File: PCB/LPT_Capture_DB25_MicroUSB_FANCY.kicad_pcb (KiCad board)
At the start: 2 copper layers, 36 x 20.8 mm, 21 parts, among them J1 USB3155-30-A, J2 DB25P064TXLF, Q1 SL2301S, Q2 SL2301S, U1 FT245RL

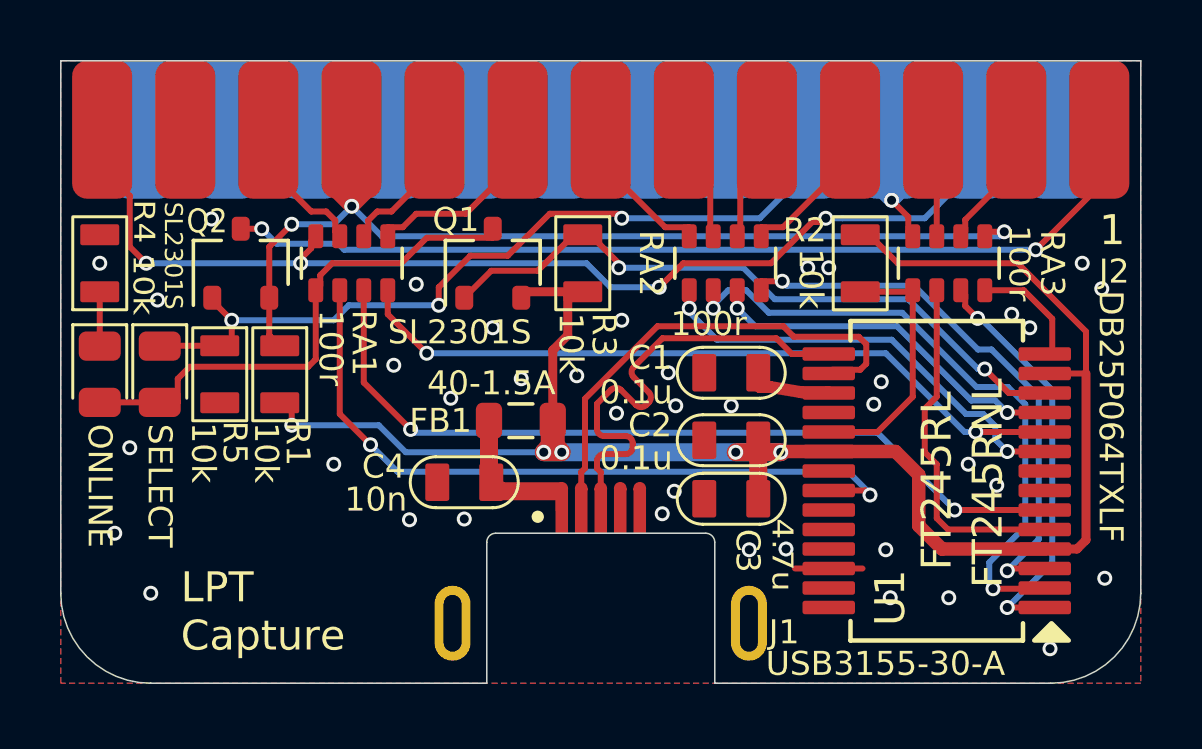
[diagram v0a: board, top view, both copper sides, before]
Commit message: fix db25_microusb_fancy filenames, pull db25_usbc_fancy into main
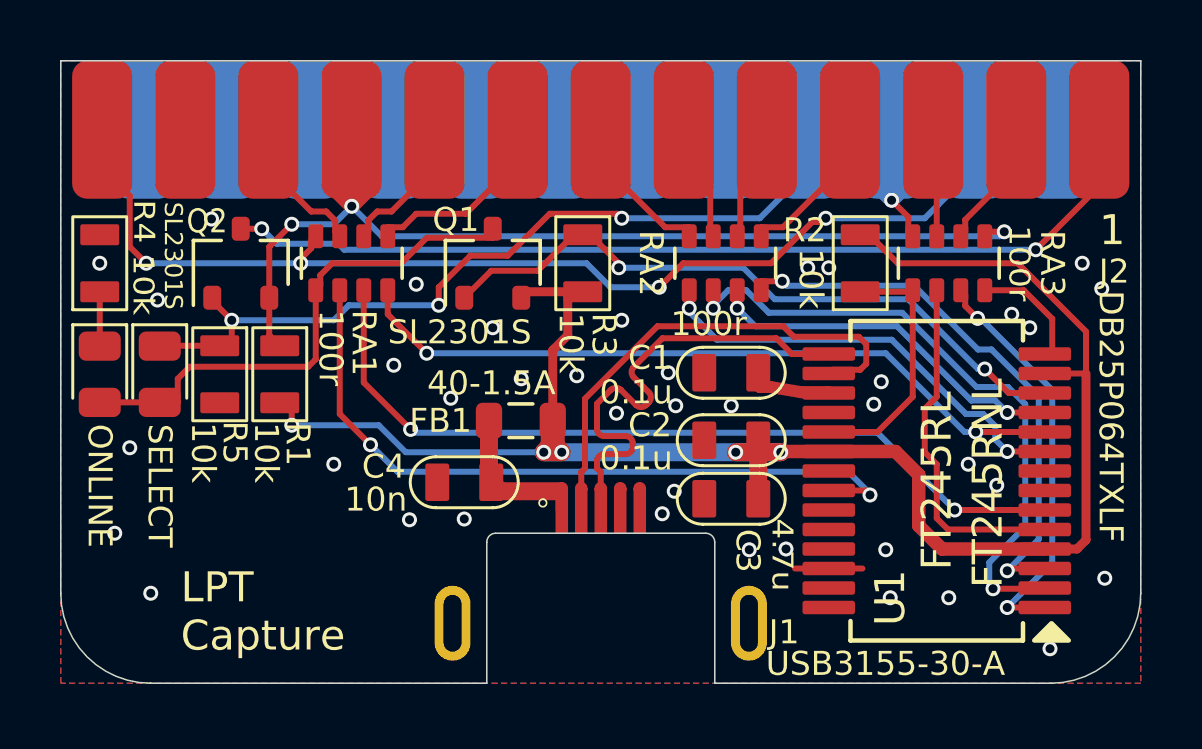
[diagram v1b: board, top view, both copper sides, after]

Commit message: pull c36_usbc_fancy into main
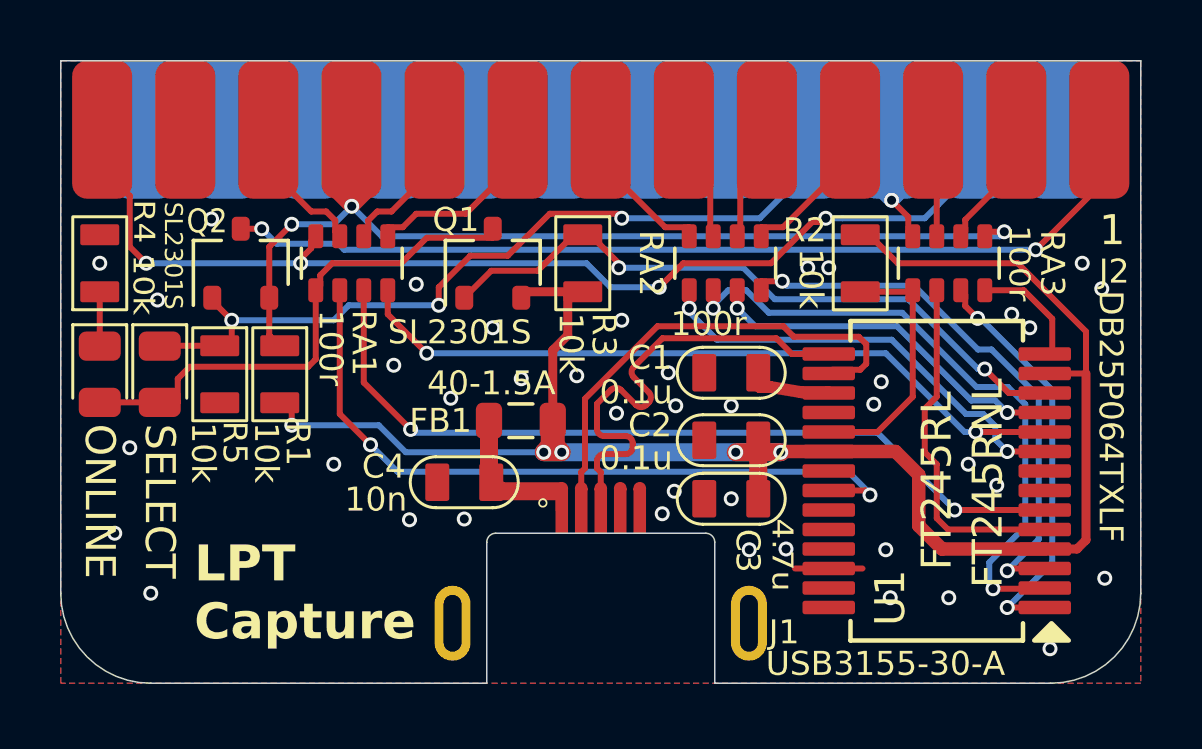
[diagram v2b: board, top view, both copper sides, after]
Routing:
- net GND: vias 39 -> 40

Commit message: db25-microusb-fancy add R6 current limit led when /SELIN driven low
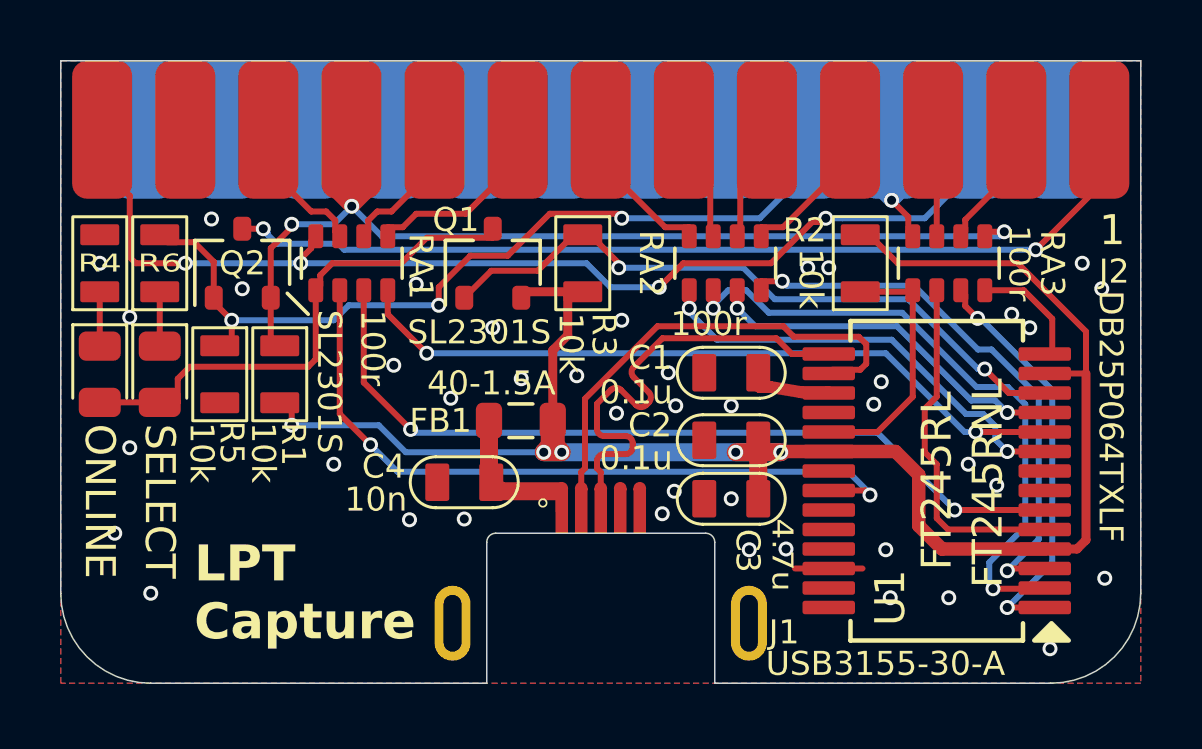
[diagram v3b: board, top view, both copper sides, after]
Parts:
- added R6: 10k, 000_LOCAL:R_0805, F.Cu at (135.3, 97.0)
- moved Q2 0.05 mm to (138.1, 97.0)
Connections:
- net /pBUSY renamed /BUSY
- net /pD0 renamed /PD0
- net /pD1 renamed /PD1
- net /pD2 renamed /PD2
- net /pD3 renamed /PD3
- net /pD4 renamed /PD4
- net /pD5 renamed /PD5
- net /pD6 renamed /PD6
- net /pD7 renamed /PD7
- net /~{pAUTOF} renamed /~{AUTOF}
- net /~{pRESET} renamed /~{INIT}
- J2 pad 1: /~{pSTROBE} -> /~{STROBE}
- J2 pad 10: /~{STROBE} -> /~{STR}
- J2 pad 13: /pONLINE -> /ONLINE
- J2 pad 15: /pONLINE -> /ONLINE
- J2 pad 17: /~{pSELIN} -> /~{SELIN}
- LED1 pad 2: /ONLINE -> /ON
- LED2 pad 1: /~{pSELIN} -> Net-(LED2-K)
- LED2 pad 2: /ONLINE -> /ON
- Q1 pad 3: /ONLINE -> /ON
- Q2 pad 1: /~{pSELIN} -> /~{SELIN}
- Q2 pad 2: /~{STROBE} -> /~{STR}
- Q2 pad 3: /~{pSTROBE} -> /~{STROBE}
- R1 pad 1: /~{STROBE} -> /~{STR}
- R5 pad 1: /~{pSELIN} -> /~{SELIN}
- RA1 pad 1: /ONLINE -> /ON
- RA1 pad 8: /pONLINE -> /ONLINE
- RA3 pad 5: /~{STROBE} -> /~{STR}
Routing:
- net /pONLINE: track 37.0 -> 0.00 mm, vias 4 -> 0
- net /~{STR}: track 0.00 -> 32.3 mm, vias 0 -> 3
- net /~{pSTROBE}: track 31.7 -> 0.00 mm, vias 2 -> 0
- net /~{SELIN}: track 0.00 -> 28.7 mm, vias 0 -> 3
- net /~{pSELIN}: track 27.4 -> 0.00 mm, vias 3 -> 0
- net /ONLINE: track 17.7 -> 37.2 mm, vias 0 -> 4
- net /ON: track 0.00 -> 17.7 mm
- net Net-(LED2-K): track 0.00 -> 1.81 mm
- net /~{STROBE}: track 32.3 -> 31.6 mm, vias 3 -> 2
- net GND: vias 40 -> 41
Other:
- board text added: "LED1, LED2: ${1d2402ba-b0f1-4368-8c52-94dfebae233b:MPN} HOUSING: ${e31e62e7-9523-48c9-88c9-8276f3149c83:VALUE} R4, R6: ${55b69257-79be-4b26-963a-95a04a5cd9dc:VALUE}"
- board text removed: "BACKSHELL: ${e31e62e7-9523-48c9-88c9-8276f3149c83:VALUE}"

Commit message: fancy versions - prevent backfeed through online led
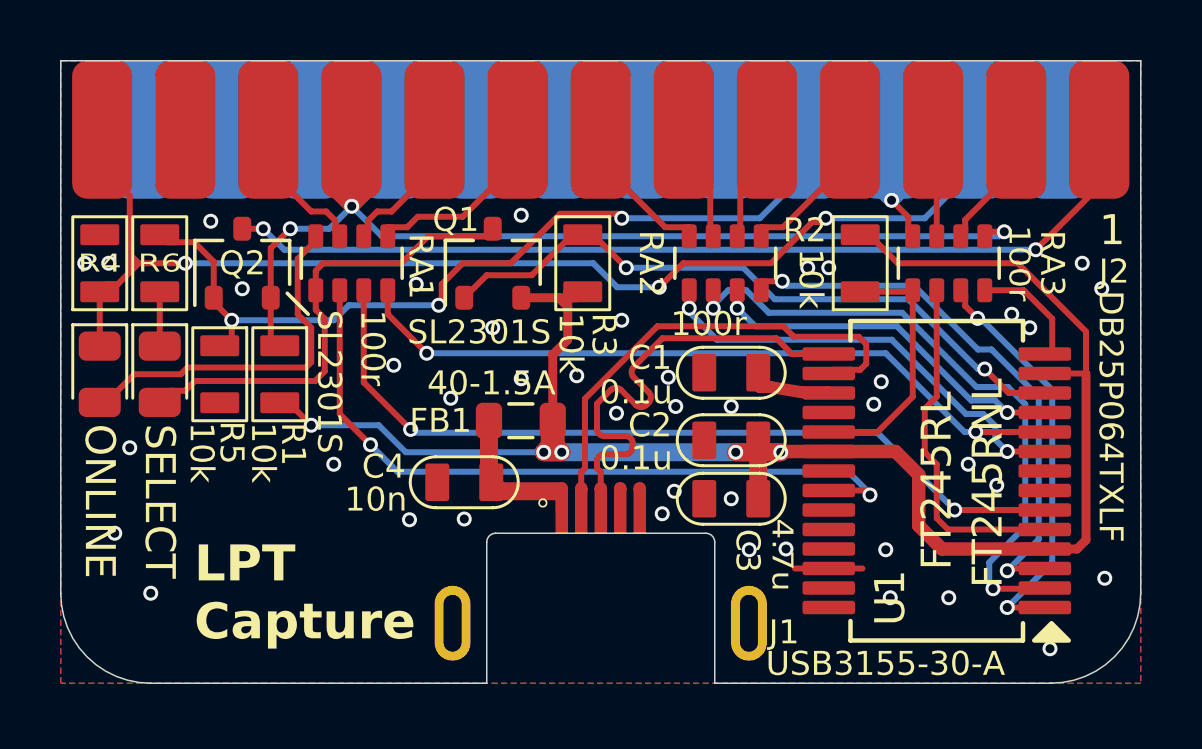
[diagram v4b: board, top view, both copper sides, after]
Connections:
- LED1 pad 1: Net-(LED1-K) -> /ONLINE
- LED1 pad 2: /ON -> Net-(LED1-A)
- R4 pad 1: Net-(LED1-K) -> /ONLINE
- RA1 pad 8: /ONLINE -> Net-(LED1-A)
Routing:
- net Net-(LED1-A): track 0.00 -> 12.2 mm
- net /ONLINE: track 37.2 -> 39.6 mm, vias 4 -> 3
- net Net-(LED1-K): track 1.81 -> 0.00 mm
- net /ON: track 17.7 -> 15.9 mm
- net GND: vias 41 -> 42
